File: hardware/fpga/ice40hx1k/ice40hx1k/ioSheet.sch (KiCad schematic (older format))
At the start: 9 parts, among them J3 Conn_01x20_Male

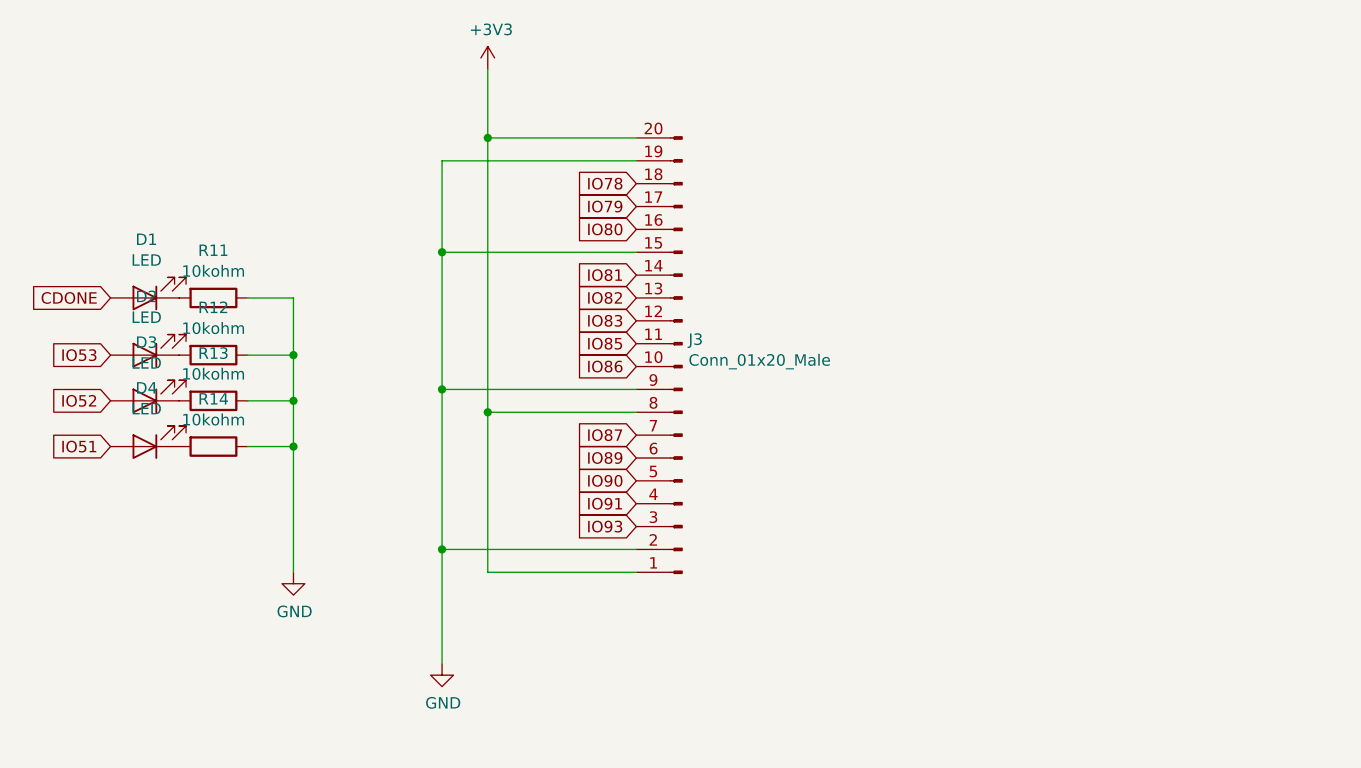
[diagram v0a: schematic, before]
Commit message: std FPGA skeleton
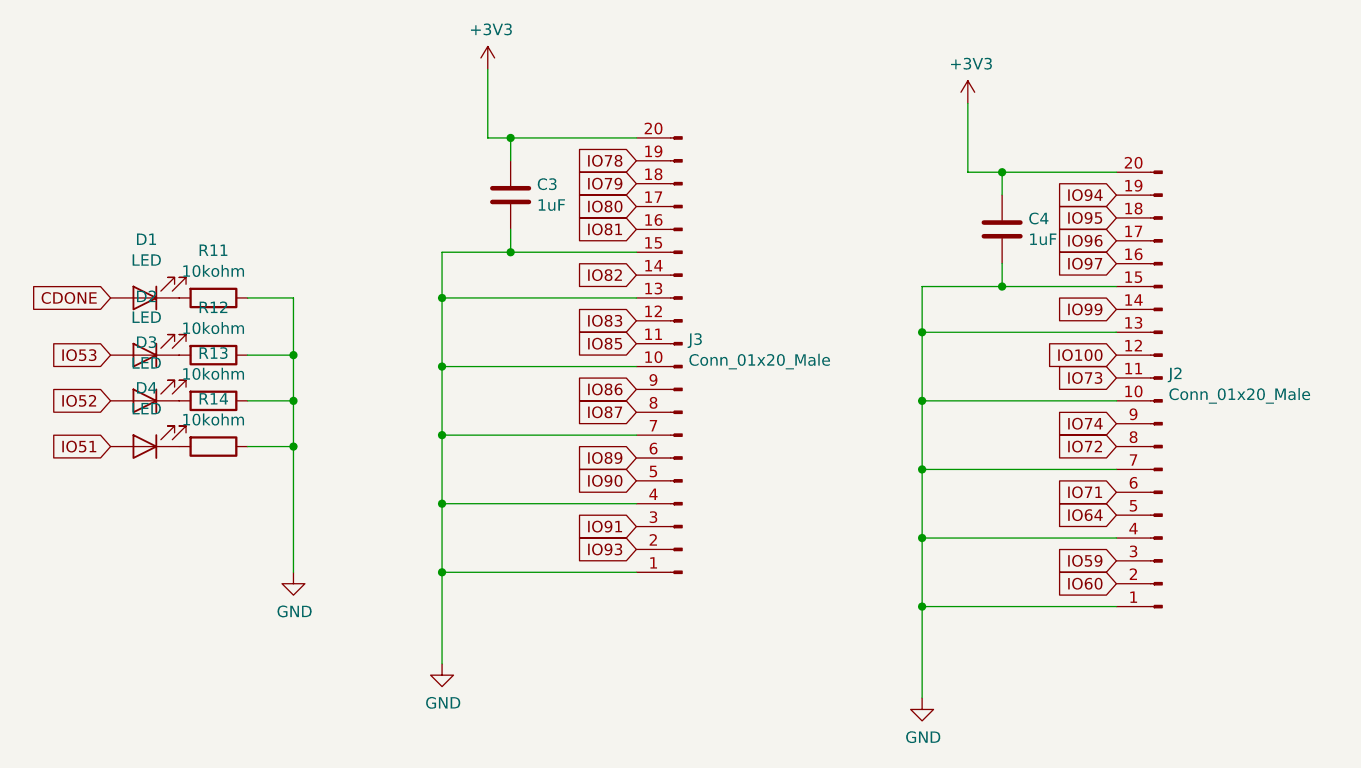
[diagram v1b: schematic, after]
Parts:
- added C3, C4: 1uF, Capacitor_SMD:C_0402_1005Metric, symbol Device:C
- added J2: Conn_01x20_Male, Connector_PinHeader_2.54mm:PinHeader_1x20_P2.54mm_Vertical, symbol Connector:Conn_01x20_Male
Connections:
- net +3V3: now also C3.1, C4.1, J2.20 (Pin_20); no longer J3.1 (Pin_1), J3.8 (Pin_8)
- net GND: now also J3.1 (Pin_1), J3.10 (Pin_10), J3.13 (Pin_13), J3.4 (Pin_4), J3.7 (Pin_7), C3.2, C4.2, J2.1 (Pin_1), J2.10 (Pin_10), J2.13 (Pin_13), J2.15 (Pin_15), J2.4 (Pin_4), J2.7 (Pin_7); no longer J3.19 (Pin_19), J3.2 (Pin_2), J3.9 (Pin_9)
- net IO78: now also J3.19 (Pin_19); no longer J3.18 (Pin_18)
- net IO79: now also J3.18 (Pin_18); no longer J3.17 (Pin_17)
- net IO80: now also J3.17 (Pin_17); no longer J3.16 (Pin_16)
- net IO81: now also J3.16 (Pin_16); no longer J3.14 (Pin_14)
- net IO82: now also J3.14 (Pin_14); no longer J3.13 (Pin_13)
- net IO86: now also J3.9 (Pin_9); no longer J3.10 (Pin_10)
- net IO87: now also J3.8 (Pin_8); no longer J3.7 (Pin_7)
- net IO91: now also J3.3 (Pin_3); no longer J3.4 (Pin_4)
- net IO93: now also J3.2 (Pin_2); no longer J3.3 (Pin_3)
- new net IO100: J2.12 (Pin_12)
- new net IO59: J2.3 (Pin_3)
- new net IO60: J2.2 (Pin_2)
- new net IO64: J2.5 (Pin_5)
- new net IO71: J2.6 (Pin_6)
- new net IO72: J2.8 (Pin_8)
- new net IO73: J2.11 (Pin_11)
- new net IO74: J2.9 (Pin_9)
- new net IO94: J2.19 (Pin_19)
- new net IO95: J2.18 (Pin_18)
- new net IO96: J2.17 (Pin_17)
- new net IO97: J2.16 (Pin_16)
- new net IO99: J2.14 (Pin_14)
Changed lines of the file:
@@
 AR Path="/5E677C12" Ref="D?"  Part="1"
 AR Path="/5E5F7D61/5E677C12" Ref="D1"  Part="1"
+AR Path="/5E9ED449/5E677C12" Ref="D1"  Part="1"
 F 0 "D1" H 2893 2745 50  0000 C CNN
 F 1 "LED" H 2893 2836 50  0000 C CNN
@@
 AR Path="/5E677C18" Ref="R?"  Part="1"
 AR Path="/5E5F7D61/5E677C18" Ref="R11"  Part="1"
+AR Path="/5E9ED449/5E677C18" Ref="R11"  Part="1"
 F 0 "R11" V 2993 3000 50  0000 C CNN
 F 1 "10kohm" V 3084 3000 50  0000 C CNN
@@
 AR Path="/5E677C20" Ref="D?"  Part="1"
 AR Path="/5E5F7D61/5E677C20" Ref="D2"  Part="1"
+AR Path="/5E9ED449/5E677C20" Ref="D2"  Part="1"
 F 0 "D2" H 2893 2995 50  0000 C CNN
 F 1 "LED" H 2893 3086 50  0000 C CNN
@@
 AR Path="/5E677C26" Ref="R?"  Part="1"
 AR Path="/5E5F7D61/5E677C26" Ref="R12"  Part="1"
+AR Path="/5E9ED449/5E677C26" Ref="R12"  Part="1"
 F 0 "R12" V 2993 3250 50  0000 C CNN
 F 1 "10kohm" V 3084 3250 50  0000 C CNN
@@
 AR Path="/5E677C2E" Ref="D?"  Part="1"
 AR Path="/5E5F7D61/5E677C2E" Ref="D3"  Part="1"
+AR Path="/5E9ED449/5E677C2E" Ref="D3"  Part="1"
 F 0 "D3" H 2893 3195 50  0000 C CNN
 F 1 "LED" H 2893 3286 50  0000 C CNN
@@
 AR Path="/5E677C34" Ref="R?"  Part="1"
 AR Path="/5E5F7D61/5E677C34" Ref="R13"  Part="1"
+AR Path="/5E9ED449/5E677C34" Ref="R13"  Part="1"
 F 0 "R13" V 2993 3450 50  0000 C CNN
 F 1 "10kohm" V 3084 3450 50  0000 C CNN
@@
 AR Path="/5E677C3C" Ref="D?"  Part="1"
 AR Path="/5E5F7D61/5E677C3C" Ref="D4"  Part="1"
+AR Path="/5E9ED449/5E677C3C" Ref="D4"  Part="1"
 F 0 "D4" H 2893 3395 50  0000 C CNN
 F 1 "LED" H 2893 3486 50  0000 C CNN
@@
 AR Path="/5E677C42" Ref="R?"  Part="1"
 AR Path="/5E5F7D61/5E677C42" Ref="R14"  Part="1"
+AR Path="/5E9ED449/5E677C42" Ref="R14"  Part="1"
 F 0 "R14" V 2993 3650 50  0000 C CNN
 F 1 "10kohm" V 3084 3650 50  0000 C CNN
@@
 	3550 3650 3550 3450
 Connection ~ 3550 3450
+Text GLabel 5050 2400 0    50   Input ~ 0
+IO78
 Text GLabel 5050 2500 0    50   Input ~ 0
-IO78
+IO79
 Text GLabel 5050 2600 0    50   Input ~ 0
-IO79
+IO80
 Text GLabel 5050 2700 0    50   Input ~ 0
-IO80
+IO81
 Text GLabel 5050 2900 0    50   Input ~ 0
-IO81
-Text GLabel 5050 3000 0    50   Input ~ 0
 IO82
 Text GLabel 5050 3100 0    50   Input ~ 0
@@
 Text GLabel 5050 3200 0    50   Input ~ 0
 IO85
-Text GLabel 5050 3300 0    50   Input ~ 0
+Text GLabel 5050 3400 0    50   Input ~ 0
 IO86
-Text GLabel 5050 3600 0    50   Input ~ 0
+Text GLabel 5050 3500 0    50   Input ~ 0
 IO87
 Text GLabel 5050 3700 0    50   Input ~ 0
@@
 Text GLabel 5050 3800 0    50   Input ~ 0
 IO90
-Text GLabel 5050 3900 0    50   Input ~ 0
+Text GLabel 5050 4000 0    50   Input ~ 0
 IO91
-Text GLabel 5050 4000 0    50   Input ~ 0
+Text GLabel 5050 4100 0    50   Input ~ 0
 IO93
 $Comp
@@
 $EndComp
 Wire Wire Line
-	4200 4600 4200 4100
-Wire Wire Line
-	4200 4100 5050 4100
-Wire Wire Line
-	5050 4200 4400 4200
-Wire Wire Line
 	4400 2000 4400 2300
 Wire Wire Line
-	4400 3500 5050 3500
-Connection ~ 4400 3500
-Wire Wire Line
-	4400 3500 4400 4200
-Wire Wire Line
-	4200 4100 4200 3400
-Wire Wire Line
-	4200 3400 5050 3400
-Connection ~ 4200 4100
-Wire Wire Line
-	4200 2400 5050 2400
-Wire Wire Line
-	4400 2300 5050 2300
-Connection ~ 4400 2300
-Wire Wire Line
-	4400 2300 4400 3500
-Wire Wire Line
-	4200 2800 5050 2800
-Connection ~ 4200 2800
-Wire Wire Line
-	4200 2800 4200 2400
-Wire Wire Line
-	4200 2800 4200 3400
-Connection ~ 4200 3400
+	4400 2300 4500 2300
+Wire Wire Line
+	5050 4200 4200 4200
+Connection ~ 4200 4200
+Wire Wire Line
+	4200 4200 4200 4600
+Wire Wire Line
+	5050 2800 4500 2800
+Wire Wire Line
+	4200 2800 4200 3000
+Wire Wire Line
+	5050 3000 4200 3000
+Connection ~ 4200 3000
+Wire Wire Line
+	4200 3000 4200 3300
+Wire Wire Line
+	5050 3300 4200 3300
+Connection ~ 4200 3300
+Wire Wire Line
+	4200 3300 4200 3600
+Wire Wire Line
+	5050 3600 4200 3600
+Connection ~ 4200 3600
+Wire Wire Line
+	4200 3600 4200 3900
+Wire Wire Line
+	5050 3900 4200 3900
+Connection ~ 4200 3900
+Wire Wire Line
+	4200 3900 4200 4200
+$Comp
+L Connector:Conn_01x20_Male J2
+U 1 1 5EABCF22
+P 7350 3450
+F 0 "J2" H 7322 3332 50  0000 R CNN
+F 1 "Conn_01x20_Male" H 7322 3423 50  0000 R CNN
+F 2 "Connector_PinHeader_2.54mm:PinHeader_1x20_P2.54mm_Vertical" H 7350 3450 50  0001 C CNN
+F 3 "~" H 7350 3450 50  0001 C CNN
+	1    7350 3450
+	-1   0    0    1
+$EndComp
+$Comp
+L power:GND #PWR0101
+U 1 1 5EABCF28
+P 6300 4750
+F 0 "#PWR0101" H 6300 4500 50  0001 C CNN
+F 1 "GND" H 6305 4577 50  0000 C CNN
+F 2 "" H 6300 4750 50  0001 C CNN
+F 3 "" H 6300 4750 50  0001 C CNN
+	1    6300 4750
+	1    0    0    -1
+$EndComp
+$Comp
+L power:+3V3 #PWR0102
+U 1 1 5EABCF2E
+P 6500 2150
+F 0 "#PWR0102" H 6500 2000 50  0001 C CNN
+F 1 "+3V3" H 6515 2323 50  0000 C CNN
+F 2 "" H 6500 2150 50  0001 C CNN
+F 3 "" H 6500 2150 50  0001 C CNN
+	1    6500 2150
+	1    0    0    -1
+$EndComp
+Wire Wire Line
+	6500 2150 6500 2450
+Wire Wire Line
+	6500 2450 6650 2450
+Wire Wire Line
+	7150 4350 6300 4350
+Connection ~ 6300 4350
+Wire Wire Line
+	6300 4350 6300 4750
+Wire Wire Line
+	7150 2950 6650 2950
+Wire Wire Line
+	6300 2950 6300 3150
+Wire Wire Line
+	7150 3150 6300 3150
+Connection ~ 6300 3150
+Wire Wire Line
+	6300 3150 6300 3450
+Wire Wire Line
+	7150 3450 6300 3450
+Connection ~ 6300 3450
+Wire Wire Line
+	6300 3450 6300 3750
+Wire Wire Line
+	7150 3750 6300 3750
+Connection ~ 6300 3750
+Wire Wire Line
+	6300 3750 6300 4050
+Wire Wire Line
+	7150 4050 6300 4050
+Connection ~ 6300 4050
+Wire Wire Line
+	6300 4050 6300 4350
+$Comp
+L Device:C C3
+U 1 1 5EAC99F6
+P 4500 2550
+F 0 "C3" H 4615 2596 50  0000 L CNN
+F 1 "1uF" H 4615 2505 50  0000 L CNN
+F 2 "Capacitor_SMD:C_0402_1005Metric" H 4538 2400 50  0001 C CNN
+F 3 "~" H 4500 2550 50  0001 C CNN
+	1    4500 2550
+	1    0    0    -1
+$EndComp
+$Comp
+L Device:C C4
+U 1 1 5EACA36E
+P 6650 2700
+F 0 "C4" H 6765 2746 50  0000 L CNN
+F 1 "1uF" H 6765 2655 50  0000 L CNN
+F 2 "Capacitor_SMD:C_0402_1005Metric" H 6688 2550 50  0001 C CNN
+F 3 "~" H 6650 2700 50  0001 C CNN
+	1    6650 2700
+	1    0    0    -1
+$EndComp
+Wire Wire Line
+	4500 2700 4500 2800
+Connection ~ 4500 2800
+Wire Wire Line
+	4500 2800 4200 2800
+Wire Wire Line
+	4500 2400 4500 2300
+Connection ~ 4500 2300
+Wire Wire Line
+	4500 2300 5050 2300
+Wire Wire Line
+	6650 2550 6650 2450
+Connection ~ 6650 2450
+Wire Wire Line
+	6650 2450 7150 2450
+Wire Wire Line
+	6650 2850 6650 2950
+Connection ~ 6650 2950
+Wire Wire Line
+	6650 2950 6300 2950
+Text GLabel 7150 2550 0    50   Input ~ 0
+IO94
+Text GLabel 7150 2650 0    50   Input ~ 0
+IO95
+Text GLabel 7150 2750 0    50   Input ~ 0
+IO96
+Text GLabel 7150 2850 0    50   Input ~ 0
+IO97
+Text GLabel 7150 3050 0    50   Input ~ 0
+IO99
+Text GLabel 7150 3250 0    50   Input ~ 0
+IO100
+Text GLabel 7150 3850 0    50   Input ~ 0
+IO71
+Text GLabel 7150 3650 0    50   Input ~ 0
+IO72
+Text GLabel 7150 3350 0    50   Input ~ 0
+IO73
+Text GLabel 7150 3550 0    50   Input ~ 0
+IO74
+Text GLabel 7150 3950 0    50   Input ~ 0
+IO64
+Text GLabel 7150 4150 0    50   Input ~ 0
+IO59
+Text GLabel 7150 4250 0    50   Input ~ 0
+IO60
 $EndSCHEMATC

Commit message: std FPGA skeleton
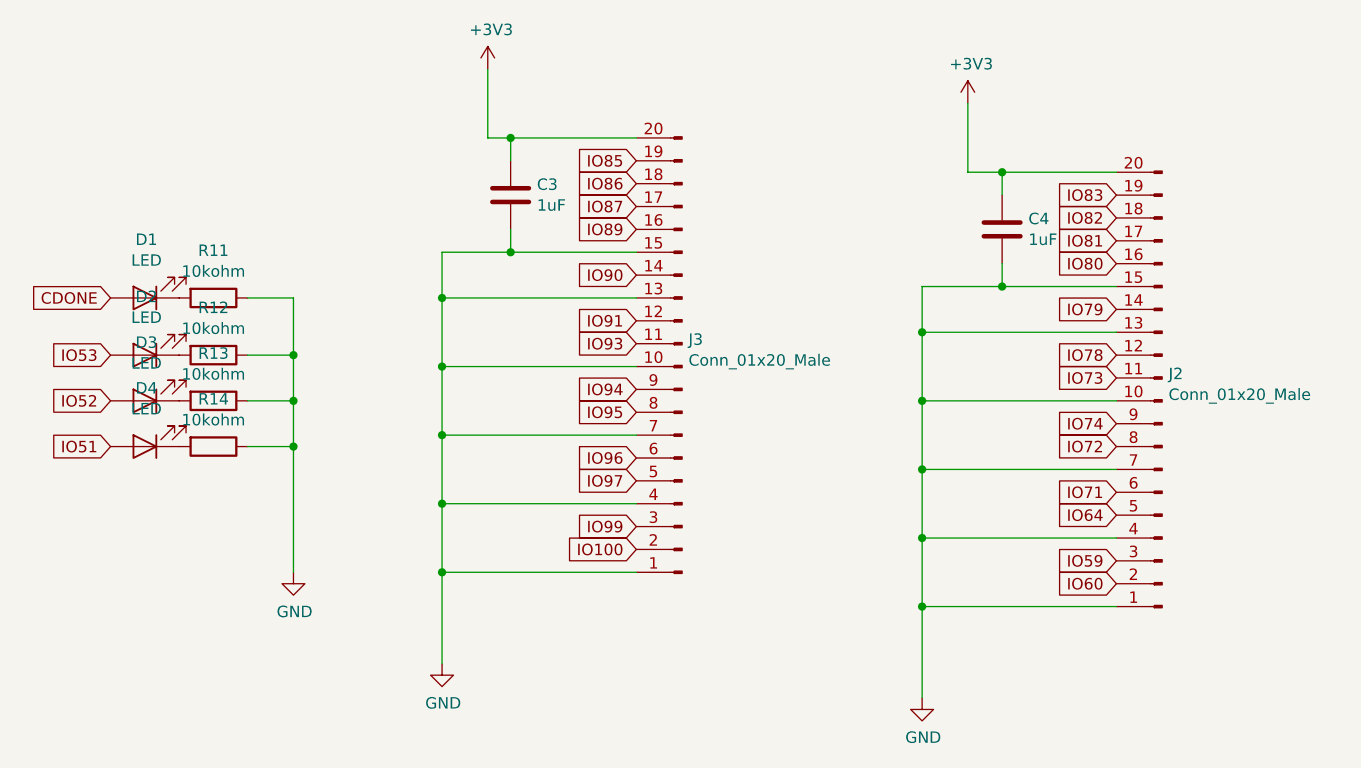
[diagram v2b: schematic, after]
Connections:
- net IO100: now also J3.2 (Pin_2); no longer J2.12 (Pin_12)
- net IO78: now also J2.12 (Pin_12); no longer J3.19 (Pin_19)
- net IO79: now also J2.14 (Pin_14); no longer J3.18 (Pin_18)
- net IO80: now also J2.16 (Pin_16); no longer J3.17 (Pin_17)
- net IO81: now also J2.17 (Pin_17); no longer J3.16 (Pin_16)
- net IO82: now also J2.18 (Pin_18); no longer J3.14 (Pin_14)
- net IO83: now also J2.19 (Pin_19); no longer J3.12 (Pin_12)
- net IO85: now also J3.19 (Pin_19); no longer J3.11 (Pin_11)
- net IO86: now also J3.18 (Pin_18); no longer J3.9 (Pin_9)
- net IO87: now also J3.17 (Pin_17); no longer J3.8 (Pin_8)
- net IO89: now also J3.16 (Pin_16); no longer J3.6 (Pin_6)
- net IO90: now also J3.14 (Pin_14); no longer J3.5 (Pin_5)
- net IO91: now also J3.12 (Pin_12); no longer J3.3 (Pin_3)
- net IO93: now also J3.11 (Pin_11); no longer J3.2 (Pin_2)
- net IO94: now also J3.9 (Pin_9); no longer J2.19 (Pin_19)
- net IO95: now also J3.8 (Pin_8); no longer J2.18 (Pin_18)
- net IO96: now also J3.6 (Pin_6); no longer J2.17 (Pin_17)
- net IO97: now also J3.5 (Pin_5); no longer J2.16 (Pin_16)
- net IO99: now also J3.3 (Pin_3); no longer J2.14 (Pin_14)
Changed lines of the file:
@@
 	3550 3650 3550 3450
 Connection ~ 3550 3450
-Text GLabel 5050 2400 0    50   Input ~ 0
-IO78
-Text GLabel 5050 2500 0    50   Input ~ 0
-IO79
-Text GLabel 5050 2600 0    50   Input ~ 0
-IO80
-Text GLabel 5050 2700 0    50   Input ~ 0
-IO81
-Text GLabel 5050 2900 0    50   Input ~ 0
-IO82
-Text GLabel 5050 3100 0    50   Input ~ 0
-IO83
-Text GLabel 5050 3200 0    50   Input ~ 0
-IO85
-Text GLabel 5050 3400 0    50   Input ~ 0
-IO86
-Text GLabel 5050 3500 0    50   Input ~ 0
-IO87
-Text GLabel 5050 3700 0    50   Input ~ 0
-IO89
-Text GLabel 5050 3800 0    50   Input ~ 0
-IO90
-Text GLabel 5050 4000 0    50   Input ~ 0
-IO91
-Text GLabel 5050 4100 0    50   Input ~ 0
-IO93
 $Comp
 L Connector:Conn_01x20_Male J3
@@
 Wire Wire Line
 	6650 2950 6300 2950
-Text GLabel 7150 2550 0    50   Input ~ 0
-IO94
-Text GLabel 7150 2650 0    50   Input ~ 0
-IO95
-Text GLabel 7150 2750 0    50   Input ~ 0
-IO96
-Text GLabel 7150 2850 0    50   Input ~ 0
-IO97
-Text GLabel 7150 3050 0    50   Input ~ 0
-IO99
-Text GLabel 7150 3250 0    50   Input ~ 0
-IO100
 Text GLabel 7150 3850 0    50   Input ~ 0
 IO71
@@
 Text GLabel 7150 4250 0    50   Input ~ 0
 IO60
+Text GLabel 7150 3250 0    50   Input ~ 0
+IO78
+Text GLabel 7150 3050 0    50   Input ~ 0
+IO79
+Text GLabel 7150 2850 0    50   Input ~ 0
+IO80
+Text GLabel 7150 2750 0    50   Input ~ 0
+IO81
+Text GLabel 7150 2650 0    50   Input ~ 0
+IO82
+Text GLabel 7150 2550 0    50   Input ~ 0
+IO83
+Text GLabel 5050 2400 0    50   Input ~ 0
+IO85
+Text GLabel 5050 2500 0    50   Input ~ 0
+IO86
+Text GLabel 5050 2600 0    50   Input ~ 0
+IO87
+Text GLabel 5050 2700 0    50   Input ~ 0
+IO89
+Text GLabel 5050 2900 0    50   Input ~ 0
+IO90
+Text GLabel 5050 3100 0    50   Input ~ 0
+IO91
+Text GLabel 5050 3200 0    50   Input ~ 0
+IO93
+Text GLabel 5050 3400 0    50   Input ~ 0
+IO94
+Text GLabel 5050 3500 0    50   Input ~ 0
+IO95
+Text GLabel 5050 3700 0    50   Input ~ 0
+IO96
+Text GLabel 5050 3800 0    50   Input ~ 0
+IO97
+Text GLabel 5050 4000 0    50   Input ~ 0
+IO99
+Text GLabel 5050 4100 0    50   Input ~ 0
+IO100
 $EndSCHEMATC

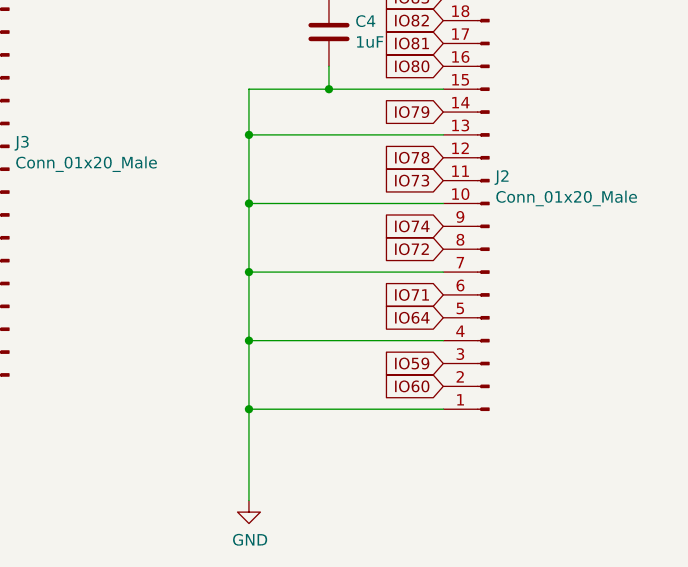
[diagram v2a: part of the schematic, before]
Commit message: std FPGA skeleton
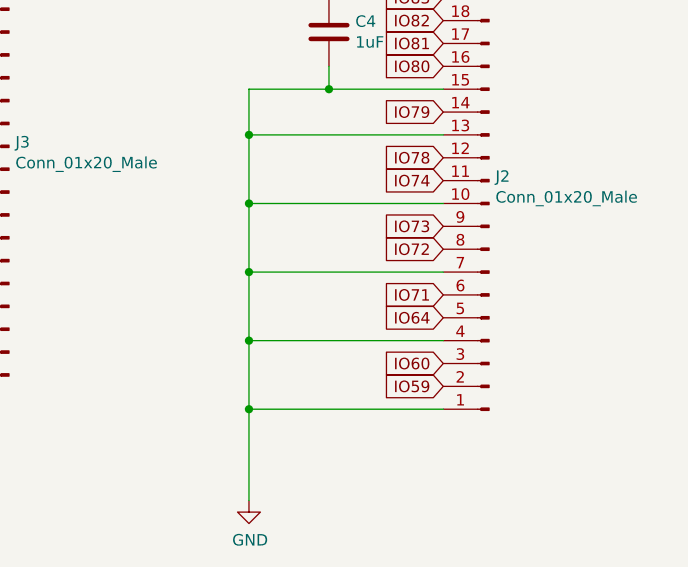
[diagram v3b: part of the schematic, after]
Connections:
- net IO59: now also J2.2 (Pin_2); no longer J2.3 (Pin_3)
- net IO60: now also J2.3 (Pin_3); no longer J2.2 (Pin_2)
- net IO73: now also J2.9 (Pin_9); no longer J2.11 (Pin_11)
- net IO74: now also J2.11 (Pin_11); no longer J2.9 (Pin_9)
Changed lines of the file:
@@
 Text GLabel 7150 3650 0    50   Input ~ 0
 IO72
+Text GLabel 7150 3550 0    50   Input ~ 0
+IO73
 Text GLabel 7150 3350 0    50   Input ~ 0
-IO73
-Text GLabel 7150 3550 0    50   Input ~ 0
 IO74
 Text GLabel 7150 3950 0    50   Input ~ 0
 IO64
+Text GLabel 7150 4250 0    50   Input ~ 0
+IO59
 Text GLabel 7150 4150 0    50   Input ~ 0
-IO59
-Text GLabel 7150 4250 0    50   Input ~ 0
 IO60
 Text GLabel 7150 3250 0    50   Input ~ 0
